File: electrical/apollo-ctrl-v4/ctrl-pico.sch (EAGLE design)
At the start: 43 parts, among them J1 ESP32-PICO-KIT, J2 DNP, J3 DNP, J6 DISPLAY_RIGHT, J7 DISPLAY_LEFT, U1 DNP (24LC01)

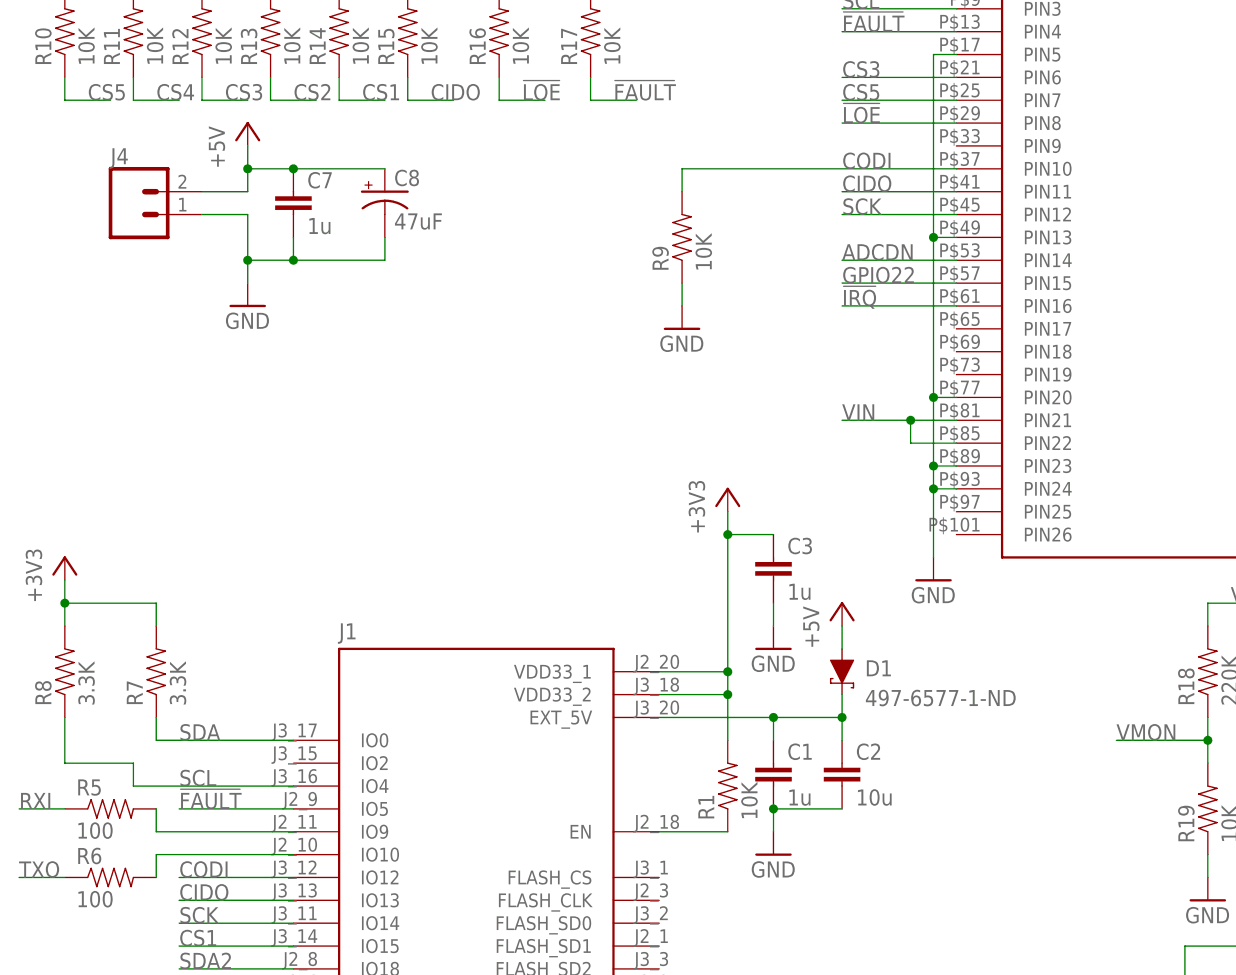
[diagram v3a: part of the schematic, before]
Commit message: Add buzzer to Apollo control board and move capacitor away from the USB port
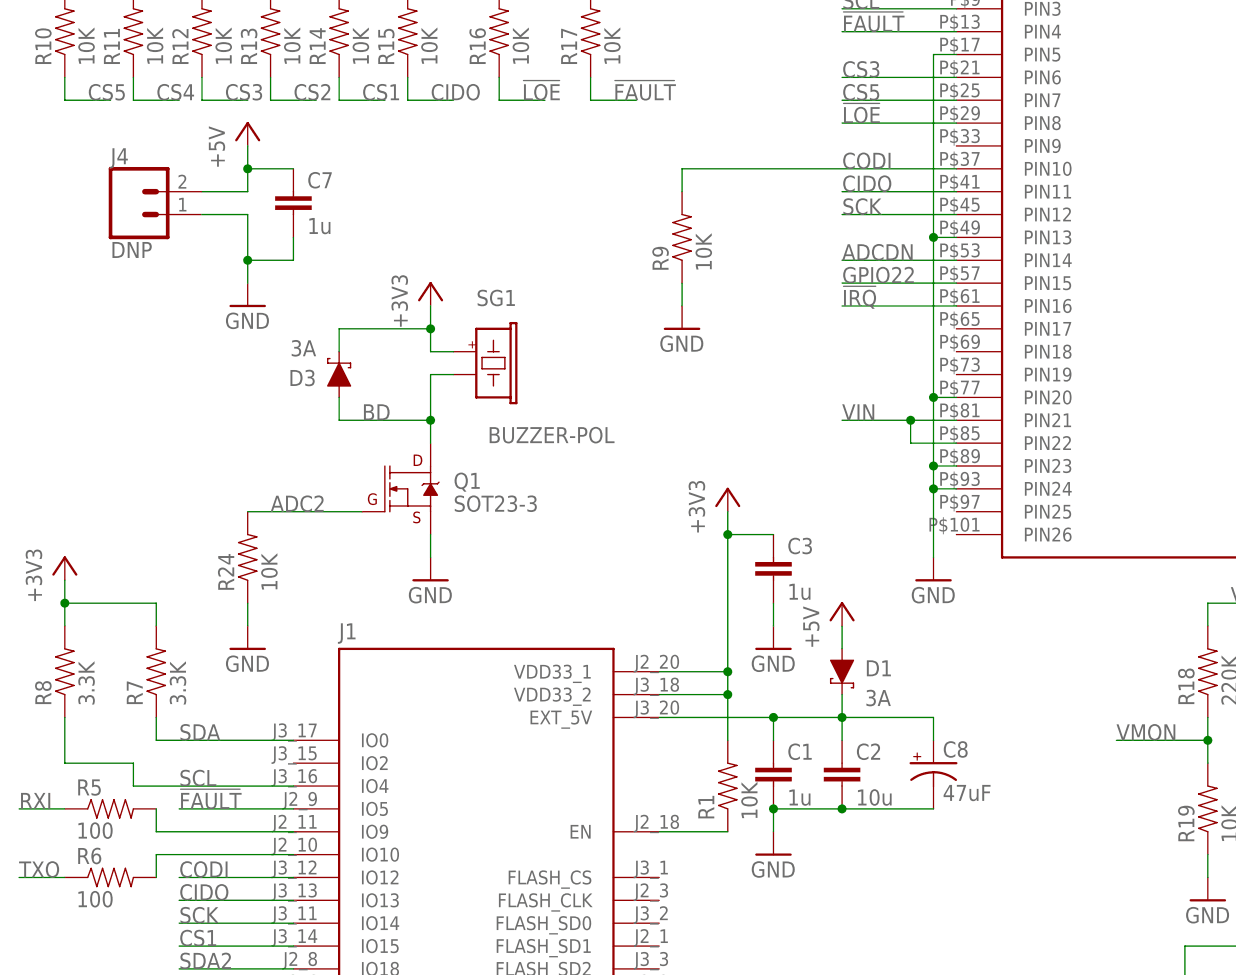
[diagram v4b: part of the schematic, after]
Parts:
- added D3: 3A, SparkFun-DiscreteSemi:DIODE-SCHOTTKY-B340A
- added Q1: SOT23-3, SparkFun-DiscreteSemi:MOSFET-NCH-AO3404A
- added R24: 10K, apollo-ctrl-v4:RESISTOR0805-RES
- added SG1: BUZZER-POL, apollo-ctrl-v4:BUZZER-POL
- D1: value 497-6577-1-ND -> 3A
- J4: value (none) -> DNP
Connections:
- new net BD: D3.A, Q1.D, SG1.N
- net +3V3: now also D3.C, SG1.P
- net +5V: no longer C8.+
- net ADC2: now also Q1.G, R24.2
- net GND: now also Q1.S, R24.1
- net USB5V: now also C8.+
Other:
- moved on the sheet: C8
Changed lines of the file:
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@@
 <part name="R1" library="apollo-ctrl-v4" deviceset="RESISTOR" device="0805-RES" value="10K"/>
 <part name="P+1" library="supply1" deviceset="+5V" device=""/>
-<part name="D1" library="SparkFun-DiscreteSemi" deviceset="DIODE-SCHOTTKY" device="-B340A" value="497-6577-1-ND"/>
+<part name="D1" library="SparkFun-DiscreteSemi" deviceset="DIODE-SCHOTTKY" device="-B340A" value="3A"/>
 <part name="C2" library="apollo-ctrl-v4" deviceset="CAP" device="0805" value="10u"/>
 <part name="C3" library="apollo-ctrl-v4" deviceset="CAP" device="0805" value="1u"/>
@@
 <part name="GND9" library="supply1" deviceset="GND" device=""/>
 <part name="FRAME2" library="frames" deviceset="LETTER_L" device=""/>
-<part name="J4" library="SparkFun-Connectors" deviceset="CONN_02" device=""/>
+<part name="J4" library="SparkFun-Connectors" deviceset="CONN_02" device="" value="DNP"/>
 <part name="P+3" library="supply1" deviceset="+5V" device=""/>
 <part name="GND14" library="supply1" deviceset="GND" device=""/>
@@
 <part name="GND16" library="supply1" deviceset="GND" device=""/>
 <part name="+3V7" library="supply1" deviceset="+3V3" device=""/>
+<part name="+3V8" library="supply1" deviceset="+3V3" device=""/>
+<part name="D3" library="SparkFun-DiscreteSemi" deviceset="DIODE-SCHOTTKY" device="-B340A" value="3A"/>
+<part name="GND15" library="supply1" deviceset="GND" device=""/>
+<part name="Q1" library="SparkFun-DiscreteSemi" deviceset="MOSFET-NCH" device="-AO3404A" value="SOT23-3"/>
+<part name="R24" library="apollo-ctrl-v4" deviceset="RESISTOR" device="0805-RES" value="10K"/>
+<part name="GND18" library="supply1" deviceset="GND" device=""/>
+<part name="SG1" library="apollo-ctrl-v4" deviceset="BUZZER-POL" device=""/>
 </parts>
 <sheets>
@@
 <attribute name="VALUE" x="34.544" y="147.701" size="1.778" layer="96"/>
 </instance>
-<instance part="C8" gate="G$1" x="43.18" y="152.4" smashed="yes">
-<attribute name="NAME" x="44.196" y="153.035" size="1.778" layer="95" font="vector"/>
-<attribute name="VALUE" x="44.196" y="148.209" size="1.778" layer="96" font="vector"/>
+<instance part="C8" gate="G$1" x="104.14" y="88.9" smashed="yes">
+<attribute name="NAME" x="105.156" y="89.535" size="1.778" layer="95" font="vector"/>
+<attribute name="VALUE" x="105.156" y="84.709" size="1.778" layer="96" font="vector"/>
 </instance>
 <instance part="+3V5" gate="G$1" x="104.14" y="182.88" smashed="yes">
@@
 <instance part="+3V7" gate="G$1" x="325.12" y="134.62" smashed="yes">
 <attribute name="VALUE" x="330.2" y="129.54" size="1.778" layer="96" rot="R90"/>
+</instance>
+<instance part="+3V8" gate="G$1" x="48.26" y="142.24" smashed="yes">
+<attribute name="VALUE" x="45.72" y="137.16" size="1.778" layer="96" rot="R90"/>
+</instance>
+<instance part="D3" gate="G$1" x="38.1" y="132.08" smashed="yes" rot="R90">
+<attribute name="NAME" x="35.56" y="132.588" size="1.778" layer="95" font="vector" rot="R180"/>
+<attribute name="VALUE" x="35.56" y="134.112" size="1.778" layer="96" font="vector" rot="R180" align="top-left"/>
+</instance>
+<instance part="GND15" gate="1" x="48.26" y="109.22" smashed="yes">
+<attribute name="VALUE" x="45.72" y="106.68" size="1.778" layer="96"/>
+</instance>
+<instance part="Q1" gate="NMOS" x="45.72" y="119.38" smashed="yes">
+<attribute name="NAME" x="50.8" y="119.38" size="1.778" layer="95" font="vector"/>
+<attribute name="VALUE" x="50.8" y="116.84" size="1.778" layer="96" font="vector"/>
+</instance>
+<instance part="R24" gate="G$1" x="27.94" y="111.76" smashed="yes" rot="R90">
+<attribute name="NAME" x="26.4414" y="107.95" size="1.778" layer="95" rot="R90"/>
+<attribute name="VALUE" x="31.242" y="107.95" size="1.778" layer="96" rot="R90"/>
+</instance>
+<instance part="GND18" gate="1" x="27.94" y="101.6" smashed="yes">
+<attribute name="VALUE" x="25.4" y="99.06" size="1.778" layer="96"/>
+</instance>
+<instance part="SG1" gate="G$1" x="53.34" y="134.62" smashed="yes" rot="R270">
+<attribute name="NAME" x="53.34" y="139.7" size="1.778" layer="95"/>
+<attribute name="VALUE" x="54.61" y="124.46" size="1.778" layer="96"/>
 </instance>
 </instances>
@@
 <wire x1="86.36" y1="83.82" x2="93.98" y2="83.82" width="0.1524" layer="91"/>
 <junction x="86.36" y="83.82"/>
+<pinref part="C8" gate="G$1" pin="-"/>
+<wire x1="93.98" y1="83.82" x2="104.14" y2="83.82" width="0.1524" layer="91"/>
+<junction x="93.98" y="83.82"/>
 </segment>
 <segment>
@@
 <pinref part="C7" gate="G$1" pin="2"/>
 <wire x1="33.02" y1="144.78" x2="33.02" y2="147.32" width="0.1524" layer="91"/>
-<pinref part="C8" gate="G$1" pin="-"/>
-<wire x1="33.02" y1="144.78" x2="43.18" y2="144.78" width="0.1524" layer="91"/>
-<wire x1="43.18" y1="144.78" x2="43.18" y2="147.32" width="0.1524" layer="91"/>
-<junction x="33.02" y="144.78"/>
 </segment>
 <segment>
@@
 <wire x1="287.02" y1="129.54" x2="287.02" y2="121.92" width="0.1524" layer="91"/>
 </segment>
+<segment>
+<pinref part="GND15" gate="1" pin="GND"/>
+<pinref part="Q1" gate="NMOS" pin="S"/>
+<wire x1="48.26" y1="111.76" x2="48.26" y2="114.3" width="0.1524" layer="91"/>
+</segment>
+<segment>
+<pinref part="GND18" gate="1" pin="GND"/>
+<pinref part="R24" gate="G$1" pin="1"/>
+<wire x1="27.94" y1="104.14" x2="27.94" y2="106.68" width="0.1524" layer="91"/>
+</segment>
 </net>
 <net name="SCK" class="0">
@@
 <wire x1="27.94" y1="154.94" x2="33.02" y2="154.94" width="0.1524" layer="91"/>
 <junction x="27.94" y="154.94"/>
-<pinref part="C8" gate="G$1" pin="+"/>
-<wire x1="33.02" y1="154.94" x2="43.18" y2="154.94" width="0.1524" layer="91"/>
-<junction x="33.02" y="154.94"/>
 </segment>
 </net>
@@
 <wire x1="93.98" y1="93.98" x2="93.98" y2="96.52" width="0.1524" layer="91"/>
 <junction x="93.98" y="93.98"/>
+<pinref part="C8" gate="G$1" pin="+"/>
+<wire x1="104.14" y1="91.44" x2="104.14" y2="93.98" width="0.1524" layer="91"/>
+<wire x1="104.14" y1="93.98" x2="93.98" y2="93.98" width="0.1524" layer="91"/>
 </segment>
 </net>
@@
 <wire x1="320.04" y1="132.08" x2="314.96" y2="132.08" width="0.1524" layer="91"/>
 </segment>
+<segment>
+<pinref part="D3" gate="G$1" pin="C"/>
+<wire x1="38.1" y1="134.62" x2="38.1" y2="137.16" width="0.1524" layer="91"/>
+<wire x1="38.1" y1="137.16" x2="48.26" y2="137.16" width="0.1524" layer="91"/>
+<pinref part="+3V8" gate="G$1" pin="+3V3"/>
+<wire x1="48.26" y1="137.16" x2="48.26" y2="139.7" width="0.1524" layer="91"/>
+<wire x1="48.26" y1="137.16" x2="48.26" y2="134.62" width="0.1524" layer="91"/>
+<junction x="48.26" y="137.16"/>
+<wire x1="48.26" y1="134.62" x2="50.8" y2="134.62" width="0.1524" layer="91"/>
+<pinref part="SG1" gate="G$1" pin="P"/>
+</segment>
 </net>
 <net name="A2" class="0">
@@
 <wire x1="20.32" y1="38.1" x2="33.02" y2="38.1" width="0.1524" layer="91"/>
 <label x="20.32" y="38.1" size="1.778" layer="95"/>
+</segment>
+<segment>
+<pinref part="Q1" gate="NMOS" pin="G"/>
+<wire x1="40.64" y1="116.84" x2="27.94" y2="116.84" width="0.1524" layer="91"/>
+<label x="30.48" y="116.84" size="1.778" layer="95"/>
+<pinref part="R24" gate="G$1" pin="2"/>
 </segment>
 </net>
@@
 </segment>
 </net>
+<net name="BD" class="0">
+<segment>
+<wire x1="50.8" y1="132.08" x2="48.26" y2="132.08" width="0.1524" layer="91"/>
+<wire x1="48.26" y1="132.08" x2="48.26" y2="127" width="0.1524" layer="91"/>
+<pinref part="D3" gate="G$1" pin="A"/>
+<wire x1="38.1" y1="129.54" x2="38.1" y2="127" width="0.1524" layer="91"/>
+<wire x1="38.1" y1="127" x2="48.26" y2="127" width="0.1524" layer="91"/>
+<label x="40.64" y="127" size="1.778" layer="95"/>
+<pinref part="Q1" gate="NMOS" pin="D"/>
+<wire x1="48.26" y1="124.46" x2="48.26" y2="127" width="0.1524" layer="91"/>
+<junction x="48.26" y="127"/>
+<pinref part="SG1" gate="G$1" pin="N"/>
+</segment>
+</net>
